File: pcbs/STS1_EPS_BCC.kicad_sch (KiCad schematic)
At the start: 52 parts, among them Q1 SI7135DP-T1-GE3, U1 LTC4020EUHFPBF, U2 SI7272DP-T1-GE3, U3 SI7272DP-T1-GE3

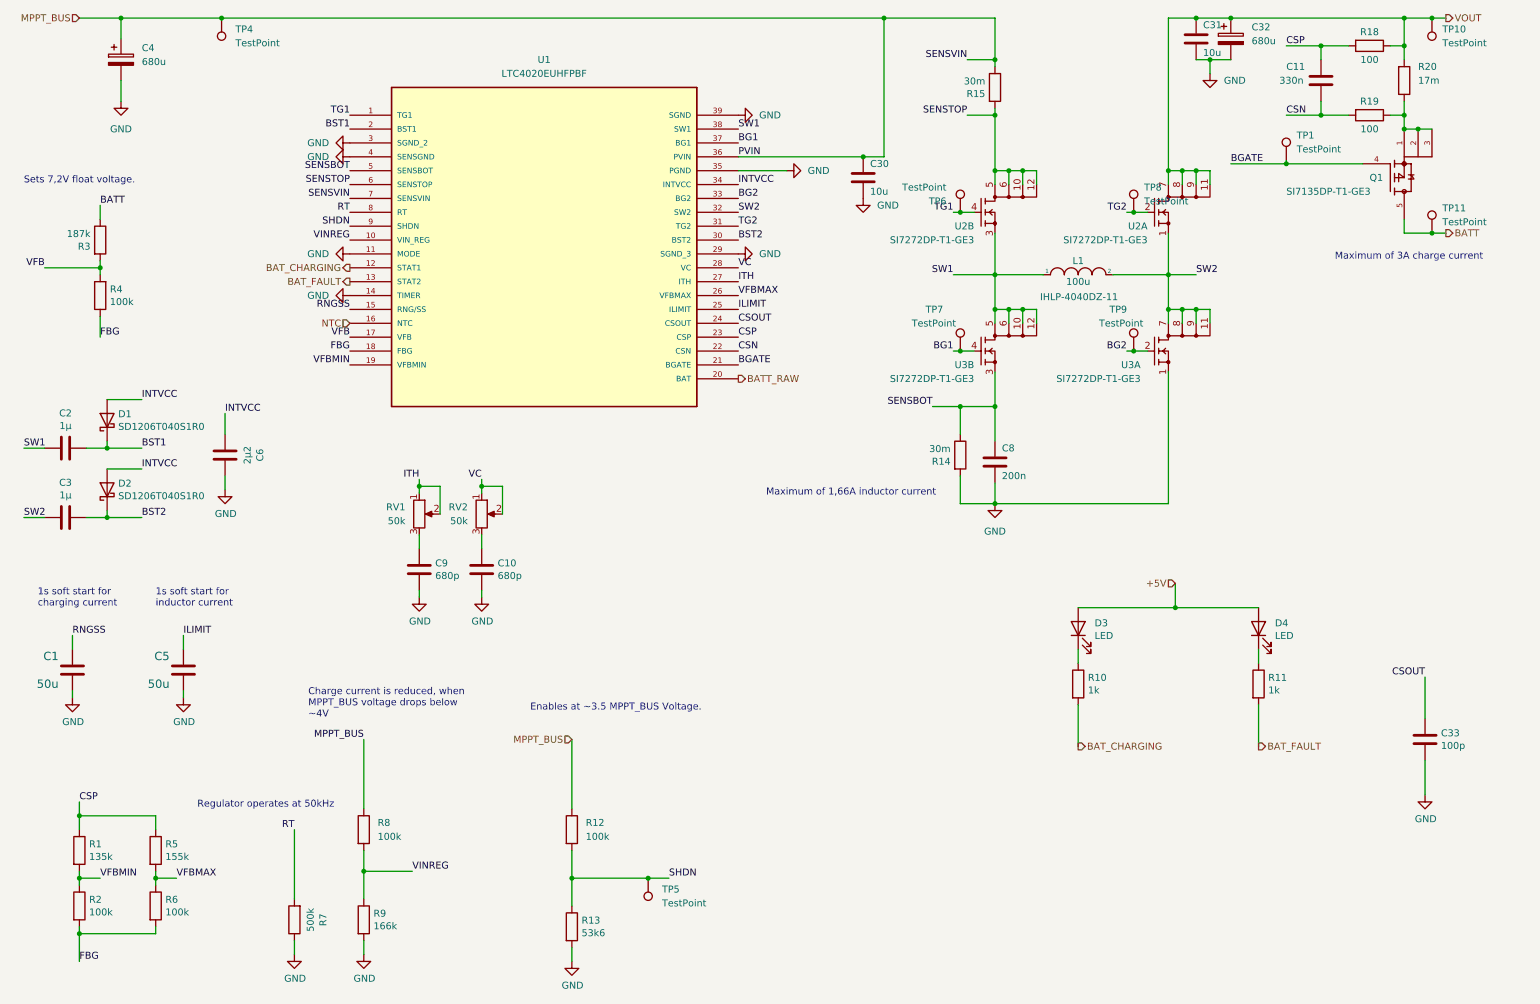
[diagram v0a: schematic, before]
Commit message: Worked on STS1_EPS_1.
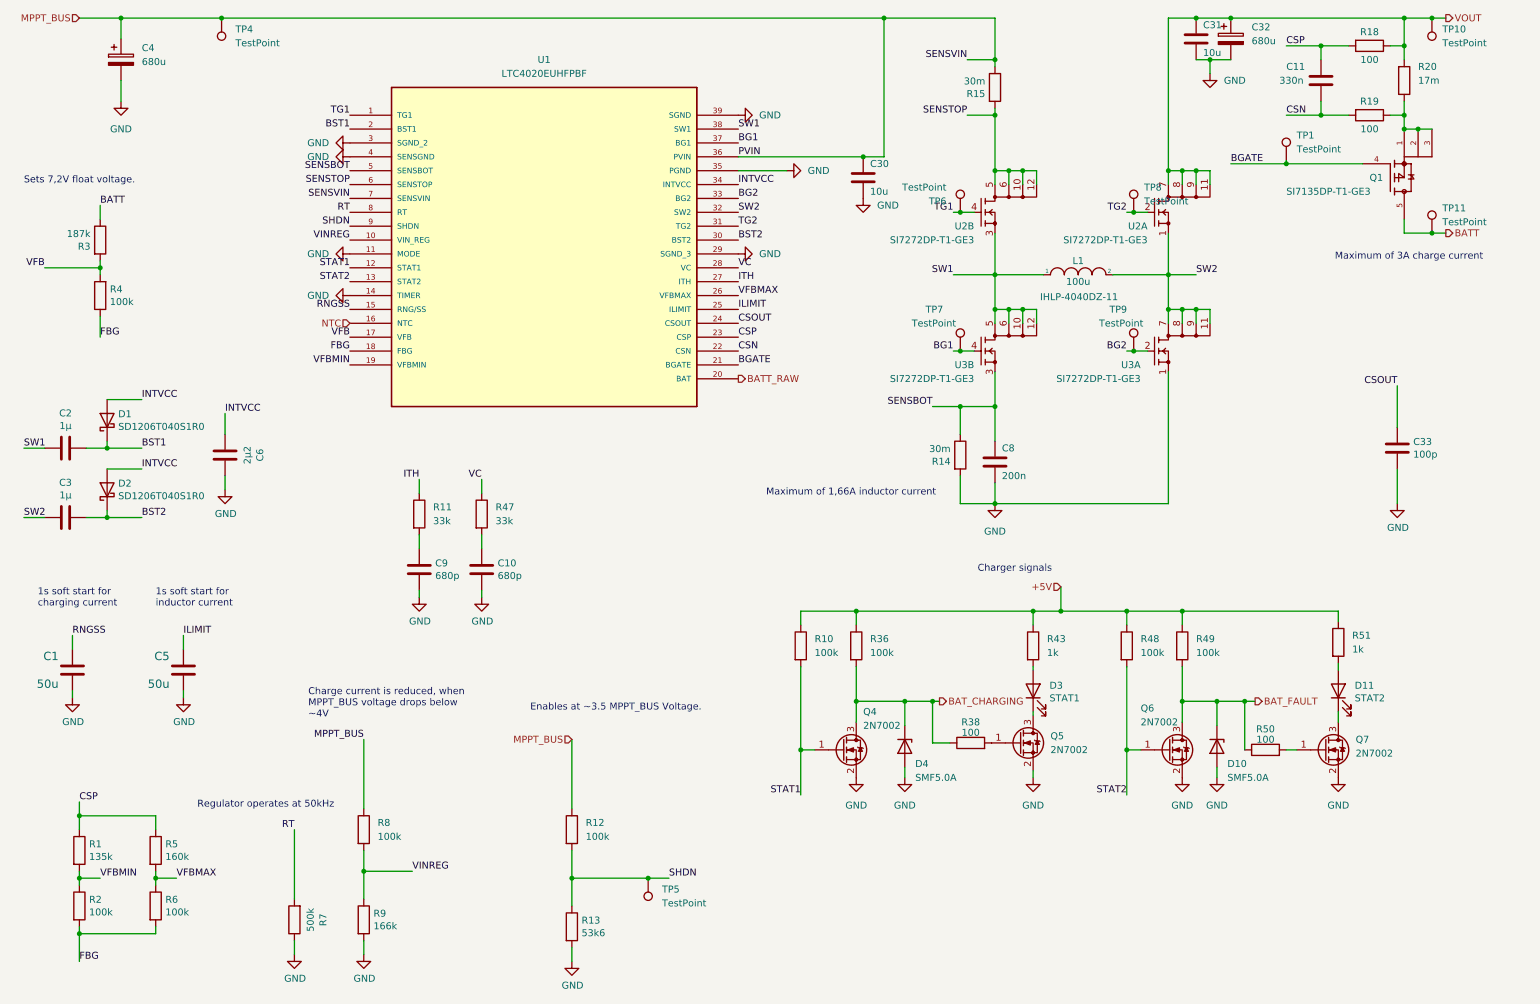
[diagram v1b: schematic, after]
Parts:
- removed D4: LED, LED_SMD:LED_0805_2012Metric, symbol Device:LED
- removed RV1, RV2: 50k, Potentiometer_SMD:Potentiometer_Bourns_TC33X_Vertical, symbol Device:R_Potentiometer
- added D10, D4: SMF5.0A, Diode_SMD:D_SMF, symbol Device:D_Zener
- added D11: STAT2, LED_SMD:LED_0805_2012Metric, symbol Device:LED
- added Q4, Q5, Q6, Q7: 2N7002, Package_TO_SOT_SMD:SOT-23, symbol Transistor_FET:2N7002
- added R36, R48, R49: 100k, Resistor_SMD:R_0805_2012Metric, symbol Device:R
- added R38, R50: 100, Resistor_SMD:R_0805_2012Metric, symbol Device:R
- added R43, R51: 1k, Resistor_SMD:R_0805_2012Metric, symbol Device:R
- added R47: 33k, Resistor_SMD:R_0805_2012Metric, symbol Device:R
- D3: value LED -> STAT1
- Q1: footprint TRANS_SI7135DP-T1-GE3 -> STS_Package_SO:POWERPAK_SO8_single
- R10: value 1k -> 100k
- R11: value 1k -> 33k
- R5: value 155k -> 160k
- U1: footprint QFN-38_UHF -> STS_Package_DFN_QFN:AD_QFN-38_UHF
- U2, U3: footprint SI7288DPT1GE3 -> STS_Package_SO:POWERPAK_SO8
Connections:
- net +5V: now also R10.1, R36.1, R43.1, R48.1, R49.1, R51.1; no longer D3.2 (A)
- net BAT_CHARGING: now also D4.1 (K), Q4.3 (D), R36.2, R38.1; no longer R10.2, U1.12 (STAT1)
- net BAT_FAULT: now also D10.1 (K), Q6.3 (D), R49.2, R50.1; no longer R11.2, U1.13 (STAT2)
- net GND: now also D10.2 (A), D4.2 (A), Q4.2 (S), Q5.2 (S), Q6.2 (S), Q7.2 (S)
- net ITH: now also R11.1
- net VC: now also R47.1
- net at C9.1: now also R11.2
- net at D3.1 (K): now also Q5.3 (D); no longer R10.1
- net at C10.1: now also R47.2
- new net: Q5.1 (G), R38.2
- new net: D11.1 (K), Q7.3 (D)
- new net: D11.2 (A), R51.2
- new net: D3.2 (A), R43.2
- new net: Q7.1 (G), R50.2
- new net STAT1: Q4.1 (G), R10.2, U1.12 (STAT1)
- new net STAT2: Q6.1 (G), R48.2, U1.13 (STAT2)
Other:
- note added: "Charger signals"
- moved on the sheet: C33, D3

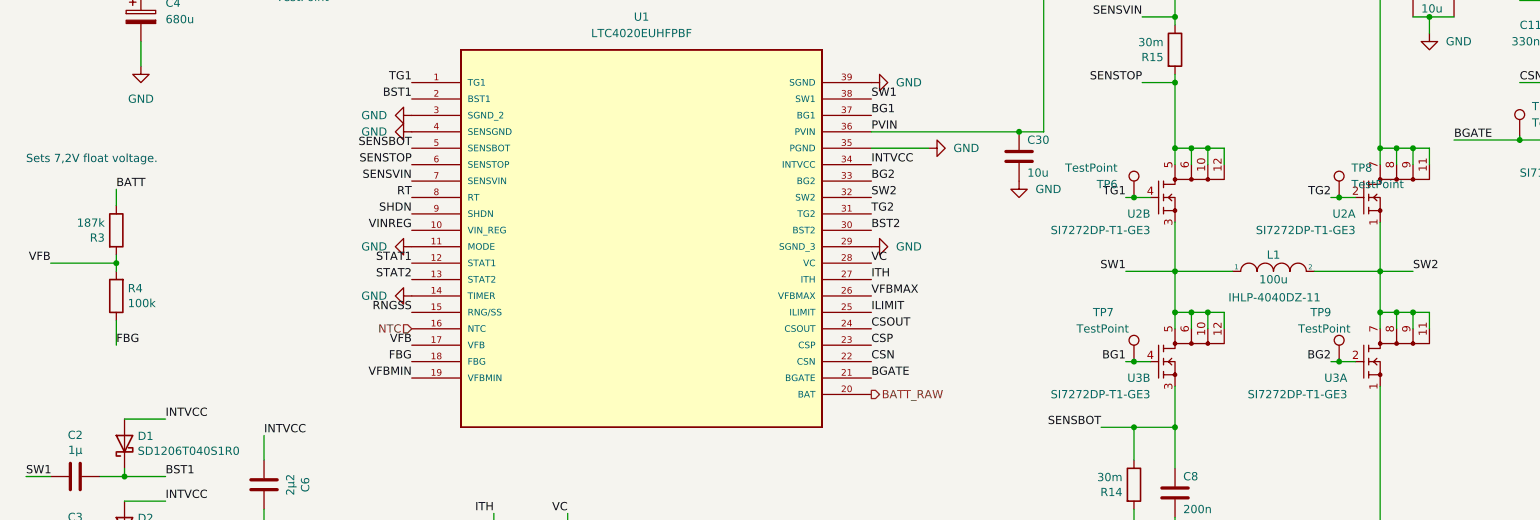
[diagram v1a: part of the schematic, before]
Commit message: Worked on STS1_EPS_1.
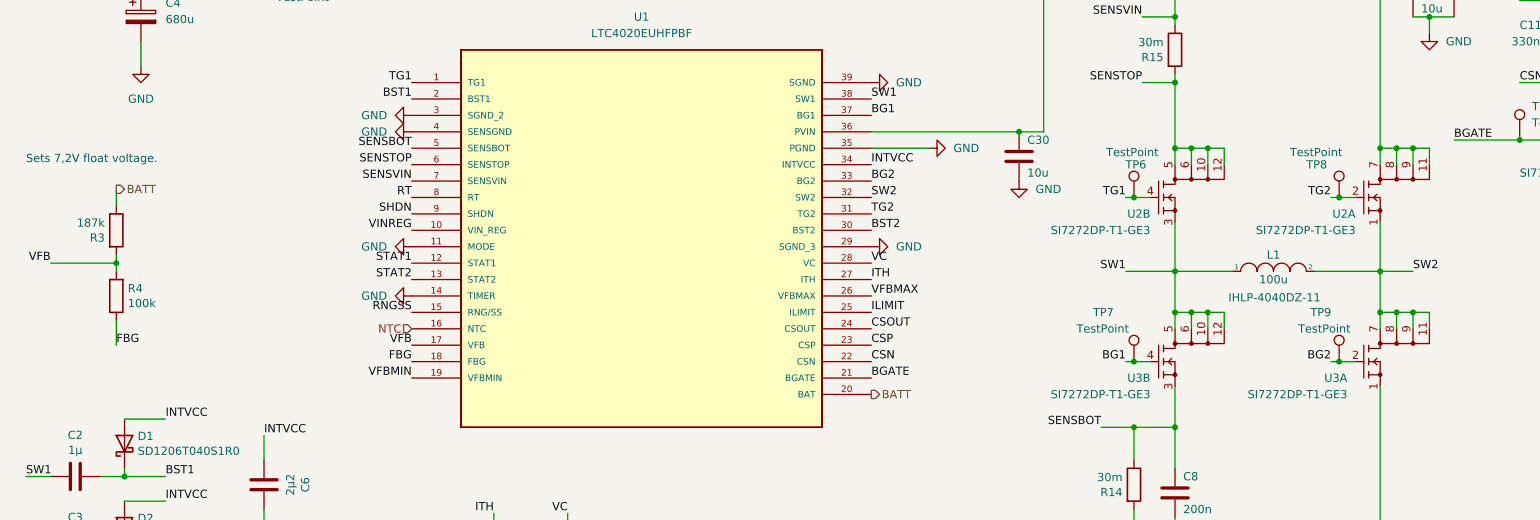
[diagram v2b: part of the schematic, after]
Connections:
- net BATT_RAW is gone; now on net BATT: U1.20 (BAT)
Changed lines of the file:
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@@
     (effects (font (size 1.27 1.27)) (justify right bottom))
-  )
-  (label "PVIN" (at 146.05 41.91 0)
-    (effects (font (size 1.27 1.27)) (justify left bottom))
   )
   (label "VFBMIN" (at 29.21 173.99 0)
@@
   (label "BST1" (at 74.93 36.83 180)
     (effects (font (size 1.27 1.27)) (justify right bottom))
-  )
-  (label "BATT" (at 29.21 50.8 0)
-    (effects (font (size 1.27 1.27)) (justify left bottom))
   )
   (label "CSN" (at 246.38 34.29 0)
@@
     (effects (font (size 1.27 1.27)) (justify left))
   )
+  (hierarchical_label "BATT" (shape output) (at 146.05 82.55 0)
+    (effects (font (size 1.27 1.27)) (justify left))
+  )
   (hierarchical_label "BAT_FAULT" (shape output) (at 240.665 141.605 0)
     (effects (font (size 1.27 1.27)) (justify left))
@@
     (effects (font (size 1.27 1.27)) (justify right))
   )
+  (hierarchical_label "BATT" (shape output) (at 29.21 50.8 0)
+    (effects (font (size 1.27 1.27)) (justify left))
+  )
   (hierarchical_label "BAT_CHARGING" (shape output) (at 182.88 141.605 0)
-    (effects (font (size 1.27 1.27)) (justify left))
-  )
-  (hierarchical_label "BATT_RAW" (shape output) (at 146.05 82.55 0)
     (effects (font (size 1.27 1.27)) (justify left))
   )
@@
   (symbol (lib_id "Connector:TestPoint") (at 186.69 52.07 0) (unit 1)
     (in_bom yes) (on_board yes)
-    (property "Reference" "TP6" (id 0) (at 184.15 50.0381 0)
-      (effects (font (size 1.27 1.27)) (justify right))
-    )
-    (property "Value" "TestPoint" (id 1) (at 184.15 47.4981 0)
+    (property "Reference" "TP6" (id 0) (at 188.595 46.99 0)
+      (effects (font (size 1.27 1.27)) (justify right))
+    )
+    (property "Value" "TestPoint" (id 1) (at 190.5 45.085 0)
       (effects (font (size 1.27 1.27)) (justify right))
     )
@@
   )
   (symbol (lib_id "Connector:TestPoint") (at 218.44 52.07 0) (unit 1)
-    (in_bom yes) (on_board yes) (fields_autoplaced)
-    (property "Reference" "TP8" (id 0) (at 220.345 47.4979 0)
-      (effects (font (size 1.27 1.27)) (justify left))
-    )
-    (property "Value" "TestPoint" (id 1) (at 220.345 50.0379 0)
-      (effects (font (size 1.27 1.27)) (justify left))
-    )
+    (in_bom yes) (on_board yes)
+    (property "Reference" "TP8" (id 0) (at 213.36 46.99 0)
+      (effects (font (size 1.27 1.27)) (justify left))
+    )
+    (property "Value" "TestPoint" (id 1) (at 210.82 45.085 0)
+      (effects (font (size 1.27 1.27)) (justify left))
+    )

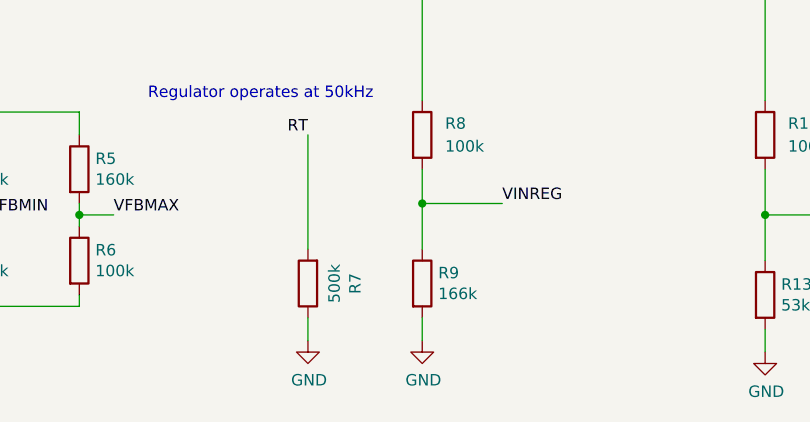
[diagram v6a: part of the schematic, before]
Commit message: Added part numbers to CSBI and inter EPS connectors. Also added some missing 3d files.
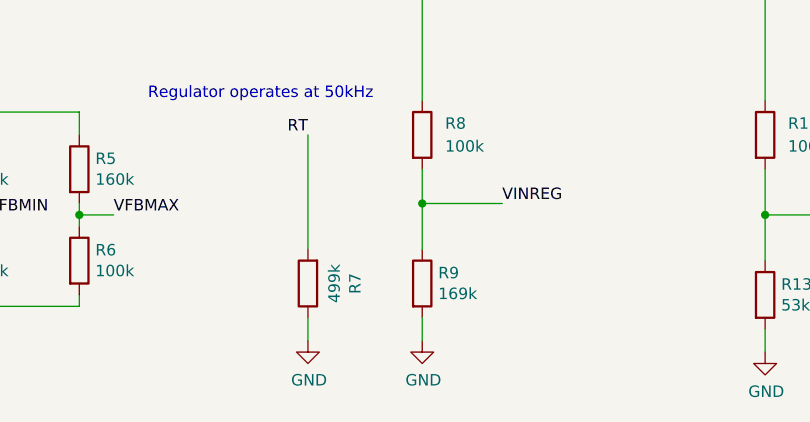
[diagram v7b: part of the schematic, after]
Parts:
- R7: value 500k -> 499k
- R9: value 166k -> 169k
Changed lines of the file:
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@@
     (in_bom yes) (on_board yes)
     (property "Reference" "R7" (id 0) (at 70.0278 181.61 90))
-    (property "Value" "500k" (id 1) (at 67.7164 181.61 90))
+    (property "Value" "499k" (id 1) (at 67.7164 181.61 90))
     (property "Footprint" "Resistor_SMD:R_0805_2012Metric" (id 2) (at 66.548 181.61 90)
       (effects (font (size 1.27 1.27)) hide)
@@
       (effects (font (size 1.27 1.27)) (justify left))
     )
-    (property "Value" "166k" (id 1) (at 79.248 182.753 0)
+    (property "Value" "169k" (id 1) (at 79.248 182.753 0)
       (effects (font (size 1.27 1.27)) (justify left))
     )
